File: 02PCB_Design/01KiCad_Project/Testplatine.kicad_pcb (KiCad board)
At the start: 4 copper layers, 201 x 100 mm, 143 parts, among them J1 MTSW-104-22-L-D-265-RA, J2 Screw_Terminal_01x03, J3 FCR7350R, J4 FCR7350R, J5 DE9_Receptacle_MountingHoles, J6 MTSW-104-22-L-D-265-RA, J7 Conn_01x06_Pin, U1 AS5047P-ATSM, U10 INA240A1PW, U11 NUCLEO-G431RB, U12 MCP2562FD, U2 ISM330BXTR, U3 L6982, U4 AP2114D, U5 LMG2100R044RARR, U6 INA240A1PW, U7 LMG2100R044RARR, U8 INA240A1PW, U9 LMG2100R044RARR

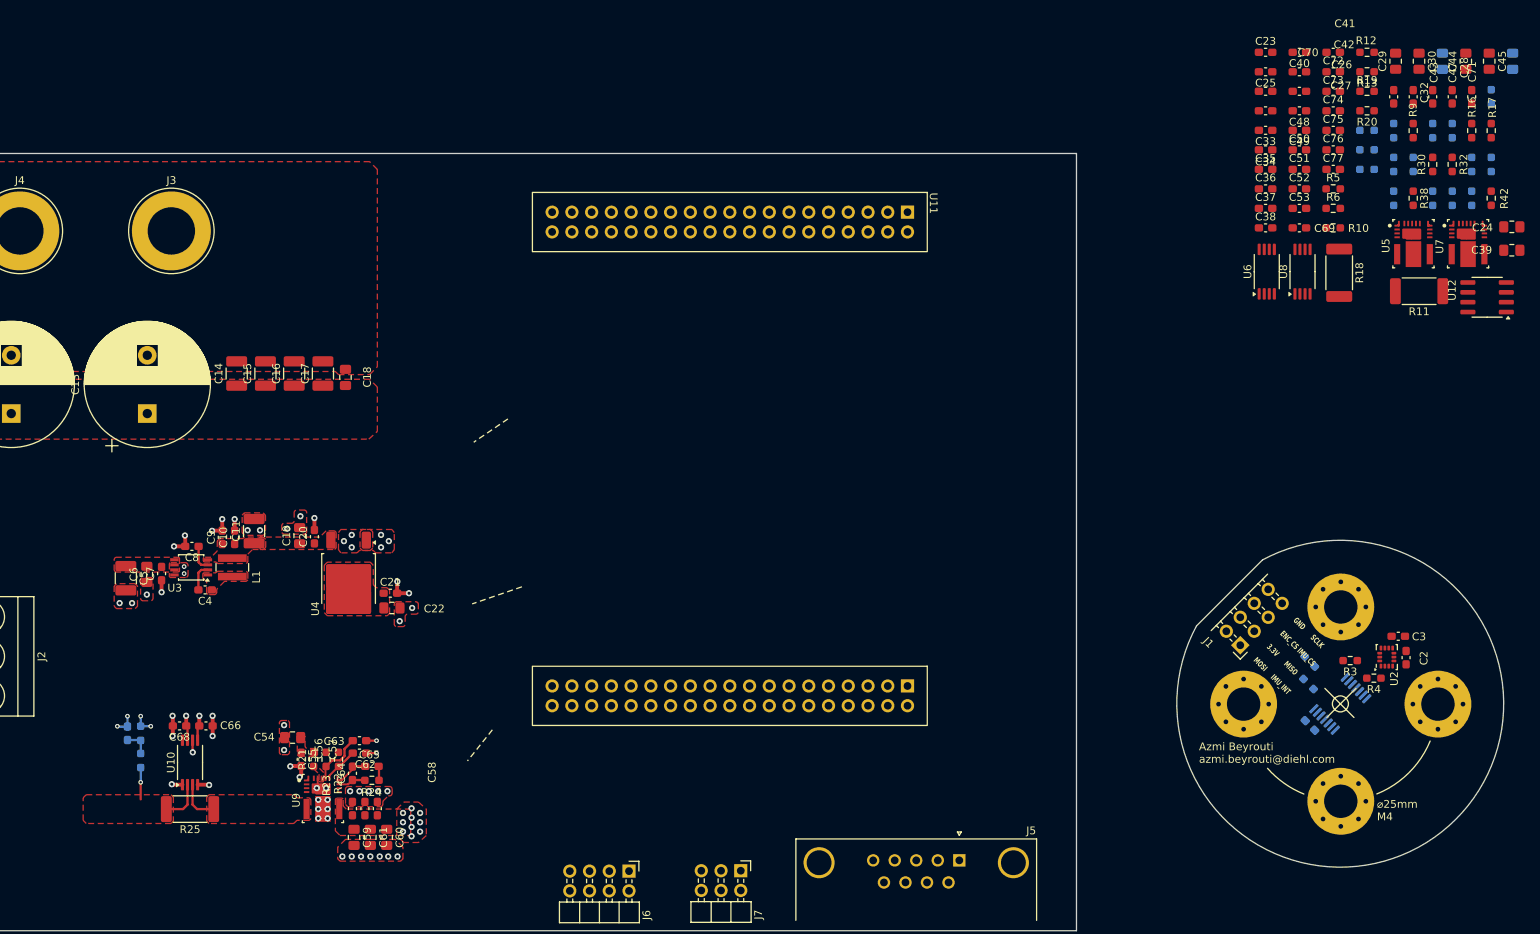
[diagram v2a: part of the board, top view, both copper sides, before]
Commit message: added plugins, copied layout
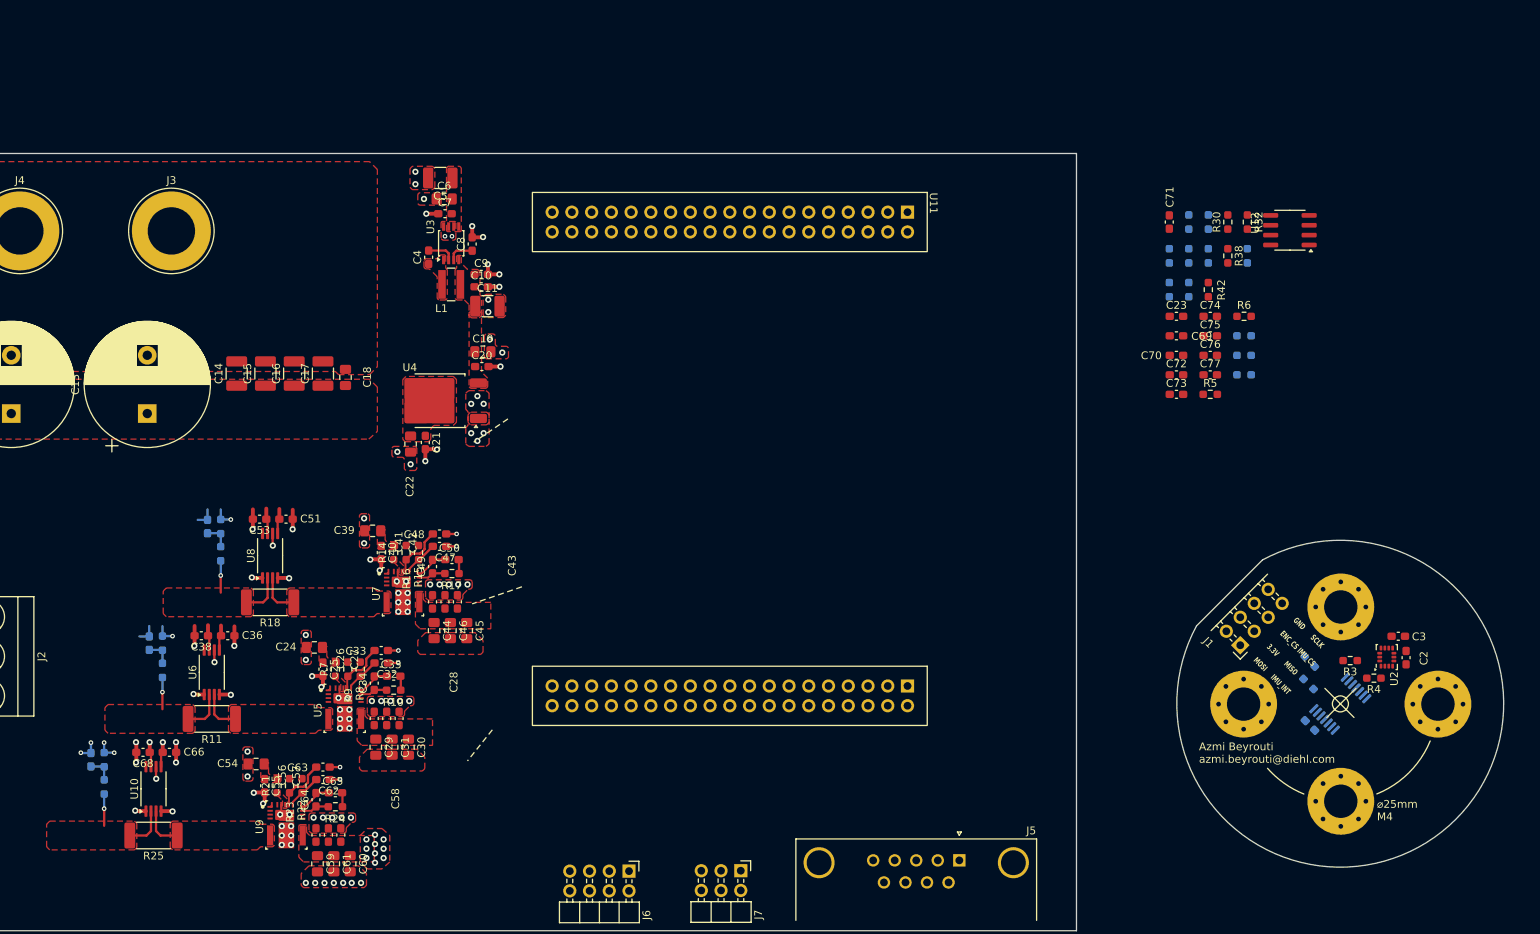
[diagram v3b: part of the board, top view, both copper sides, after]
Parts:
- C31, C46, R14, R15, R7, R8: moved to F.Cu
- C37, C52, R12, R13, R19, R20: moved to B.Cu
- moved R12 174.2 mm to (72.2, 106.0), turned to 90 degrees
- moved R13 171.5 mm to (72.2, 102.5), turned to 90 degrees
- moved R7 165.9 mm to (94.4, 105.8)
- moved R11 164.8 mm to (78.5, 112.2)
- moved C24 163.3 mm to (91.7, 103.0)
- moved C31 161.4 mm to (101.7, 115.8)
- moved R19 159.0 mm to (79.7, 91.0), turned to 90 degrees
- moved C29 158.1 mm to (99.6, 115.8), turned to -90 degrees
- moved C30 157.1 mm to (103.8, 115.8)
- moved R20 156.9 mm to (79.7, 87.5), turned to 90 degrees
- moved C46 155.1 mm to (109.2, 100.8)
- moved C37 154.1 mm to (70.5, 102.5), turned to 90 degrees
- moved R9 153.6 mm to (96.0, 105.8), turned to -90 degrees
- moved C44 151.6 mm to (107.1, 100.8), turned to -90 degrees
- moved C32 151.4 mm to (100.3, 105.0), turned to 0 degrees
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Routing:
- net GNDA: track 35.0 -> 78.5 mm, vias 57 -> 95
- net +3.3V: track 6.63 -> 19.6 mm
- net /escSheet/HalfBridgePowerStage2/PH_OUT: track 0.00 -> 9.61 mm, vias 0 -> 1
- net /escSheet/HalfBridgePowerStage1/PH_OUT: track 0.00 -> 9.61 mm, vias 0 -> 1
- net Net-(U5-LI): track 0.00 -> 7.22 mm
- net Net-(U7-LI): track 0.00 -> 7.22 mm
- net /escSheet/HalfBridgePowerStage2/SW: track 0.00 -> 5.53 mm
- net /escSheet/HalfBridgePowerStage1/SW: track 0.00 -> 5.53 mm
- net Net-(U7-HS): track 0.00 -> 4.60 mm
- net Net-(U5-HS): track 0.00 -> 4.60 mm
- net Net-(U7-HI): track 0.00 -> 4.56 mm
- net Net-(U5-HI): track 0.00 -> 4.56 mm
- net Net-(U7-HB): track 0.00 -> 3.53 mm
- net Net-(U5-HB): track 0.00 -> 3.53 mm
- net /escSheet/HalfBridgePowerStage2/V_PHASE: track 0.00 -> 3.40 mm
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- added copper zone on F.Cu, net /escSheet/HalfBridgePowerStage1/PH_OUT
- added copper zone on F.Cu, net /escSheet/HalfBridgePowerStage1/SW
- added copper zone on F.Cu, net /escSheet/HalfBridgePowerStage2/PH_OUT
- added copper zone on F.Cu, net /escSheet/HalfBridgePowerStage2/SW
- added copper zone on F.Cu, net Net-(U5-VCC)
- added copper zone on F.Cu, net Net-(U7-VCC)

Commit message: sensor sheet & Power delivery
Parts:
- removed J1: MTSW-104-22-L-D-265-RA, Connector_PinHeader_2.54mm:PinHeader_2x04_P2.54mm_Horizontal
- added J8: RJ45-8N-B, RJ45-8N-B:TE_RJ45-8N-B, B.Cu at (229.8, 96.5)
- C1, R1: moved to F.Cu
- moved C26 180.3 mm to (271.6, 58.7)
- moved C28 180.3 mm to (274.8, 58.7)
- moved C29 180.3 mm to (271.8, 62.4)
- moved C34 180.3 mm to (271.6, 54.2)
- moved C35 180.3 mm to (274.1, 53.3)
- moved R10 180.3 mm to (274.1, 55.1)
- moved R7 180.3 mm to (266.6, 52.4)
- moved R8 180.3 mm to (269.8, 52.4)
- moved U5 180.3 mm to (267.8, 57.4)
- moved C24 180.3 mm to (263.9, 49.6)
- moved C25 180.3 mm to (265.0, 52.4)
- moved C27 180.3 mm to (273.2, 58.7)
- moved C30 180.3 mm to (276.0, 62.4)
- moved C31 180.3 mm to (273.9, 62.4)
- moved C32 180.3 mm to (272.5, 51.6)
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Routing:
- net /SensorSheet/SPI_MOSI: track 0.00 -> 37.7 mm, vias 0 -> 1
- net /SensorSheet/SPI_SCLK: track 0.00 -> 37.3 mm, vias 0 -> 1
- net /SensorSheet/SPI_MISO: track 0.00 -> 33.8 mm, vias 0 -> 1
- net /SensorSheet/IMU_INT1: track 0.00 -> 22.0 mm, vias 0 -> 2
- net /SensorSheet/ENC_CS: track 0.00 -> 18.0 mm, vias 0 -> 2
- net /SensorSheet/IMU_CS: track 0.00 -> 17.7 mm, vias 0 -> 1
- net GND1: track 0.00 -> 11.5 mm, vias 0 -> 8
- net +3.3VP: track 0.00 -> 11.1 mm, vias 0 -> 5
- net Net-(U1-MISO): track 0.00 -> 1.86 mm
- net Net-(U2-SDO/TA0): track 0.00 -> 1.48 mm
- added copper zone on In2.Cu, net +24V
- added copper zone on B.Cu, net +3.3VP
- added copper zone on F.Cu, net +3.3VP
- added copper zone on In2.Cu, net +3.3VP
- added copper zone on B.Cu, net GND1
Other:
- board size 201 x 100 mm -> 217.9 x 112.1 mm
- board text added: "Falsch Herum?"
- board text removed: "Azmi Beyrouti azmi.beyrouti@diehl.com"
- board text removed: "GND ENC_CS 3.3V MOSI"
- board text removed: "SCLK IMU_CS MISO IMU_INT"
- board text removed: "⌀25mm M4"

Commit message: revised halfbridge 24V input
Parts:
- moved C61 53.3 mm to (102.4, 117.2), turned to 0 degrees
- moved R22 53.2 mm to (100.1, 107.4)
- moved R23 53.1 mm to (96.9, 107.4)
- moved C56 53.1 mm to (102.2, 113.9), turned to 0 degrees
- moved C62 52.3 mm to (101.7, 107.4), turned to 90 degrees
- moved C54 52.2 mm to (92.6, 105.5)
- moved C66 52.2 mm to (81.3, 104.0)
- moved C68 52.2 mm to (77.9, 104.0)
- moved C67 52.2 mm to (71.2, 105.0)
- moved R25 52.2 mm to (79.3, 114.7)
- moved R26 52.2 mm to (72.9, 108.5)
- moved R27 52.2 mm to (72.9, 105.0)
- moved U10 52.2 mm to (79.3, 108.7)
- moved U9 52.2 mm to (96.4, 113.4)
- moved C55 52.2 mm to (93.6, 108.3)
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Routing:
- net Net-(U9-LI): track 7.22 -> 4.18 mm
- net +3.3VP: track 11.1 -> 12.5 mm, vias 5 -> 6
- net Net-(U9-HI): track 4.56 -> 5.50 mm
- net Net-(U9-HS): track 4.60 -> 4.09 mm
- net GNDA: track 78.5 -> 78.4 mm, vias 95 -> 100
- net +24V: vias 28 -> 27
